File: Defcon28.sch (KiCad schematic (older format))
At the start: 10 parts

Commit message: Added regulators
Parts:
- added C? (x6): 1μF, symbol Device:C_Small
- added D?: LED_ALT, symbol Device:LED_ALT
- added R?: R_Small_US, symbol Device:R_Small_US
- added SW?: SW_SP4T, symbol Defcon28:SW_SP4T
- added U?: MCP1826S-1802E_DB, symbol Defcon28:MCP1826S-1802E_DB
- added U?: MCP1825ST-2502E_DB, symbol Defcon28:MCP1825ST-2502E_DB
- added U?: MCP1825ST-3302E_DB, symbol Defcon28:MCP1825ST-3302E_DB
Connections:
- net GND: now also C?.2, C?.2, C?.2, C?.2, C?.2, C?.2, D?.1 (K), U?.2 (GND), U?.2 (GND), U?.2 (GND)
- net VBUS: now also C?.1, C?.1, C?.1, R?.1, SW?.5, U?.1 (VIN), U?.1 (VIN), U?.1 (VIN)
- net VCC: now also SW?.3
- new net: D?.2 (A), R?.2
- new net +1V8: C?.1, SW?.1, U?.3 (VOUT)
- new net +2V5: C?.1, SW?.2, U?.3 (VOUT)
- new net +3V3: C?.1, SW?.4, U?.3 (VOUT)
- no-connect marks 7 -> 11
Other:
- moved on the sheet: D?

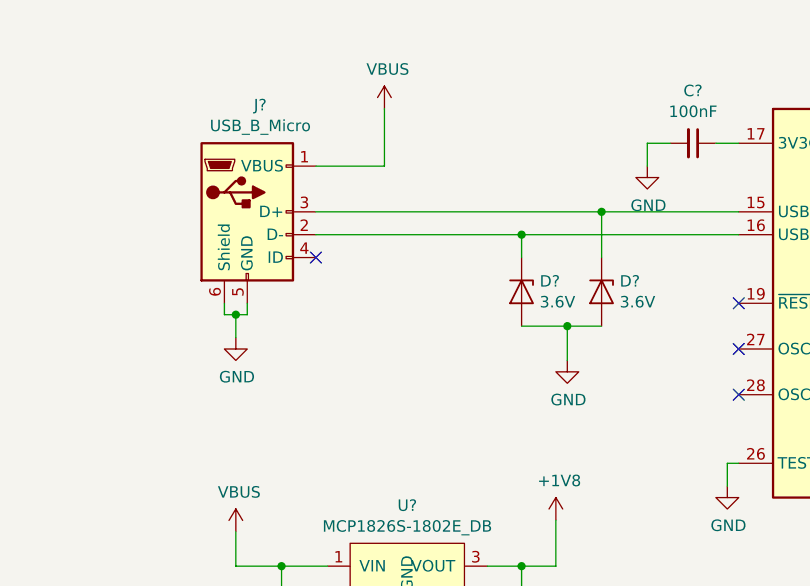
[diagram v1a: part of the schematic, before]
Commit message: Added input cap
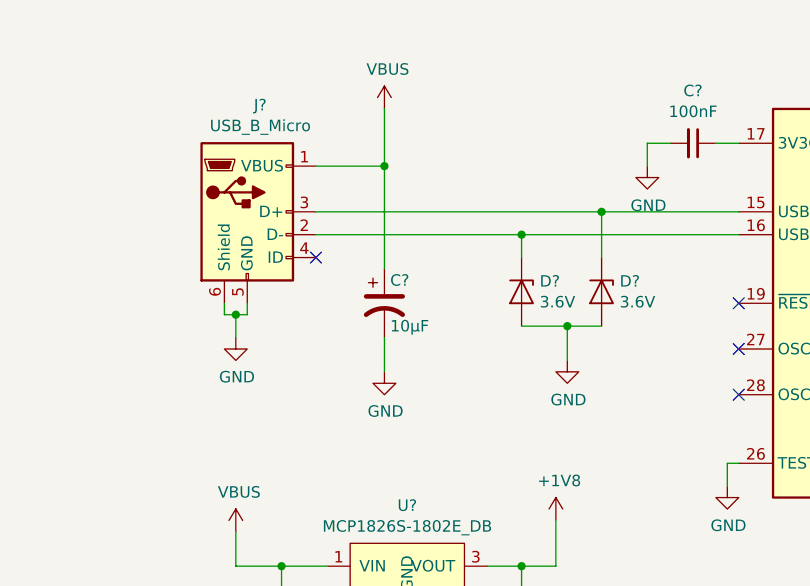
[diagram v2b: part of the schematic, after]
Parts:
- added C?: 10µF, symbol Device:CP1
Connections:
- net GND: now also C?.2
- net VBUS: now also C?.1
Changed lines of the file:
@@
 Wire Wire Line
 	3700 7350 3200 7350
+$Comp
+L Device:CP1 C?
+U 1 1 5E38AA29
+P 3100 3400
+F 0 "C?" H 3125 3500 50  0000 L CNN
+F 1 "10µF" H 3125 3300 50  0000 L CNN
+F 2 "" H 3100 3400 50  0001 C CNN
+F 3 "~" H 3100 3400 50  0001 C CNN
+	1    3100 3400
+	1    0    0    -1
+$EndComp
+Wire Wire Line
+	3100 3250 3100 2800
+Connection ~ 3100 2800
+$Comp
+L power:GND #PWR?
+U 1 1 5E38F14C
+P 3100 3700
+F 0 "#PWR?" H 3100 3450 50  0001 C CNN
+F 1 "GND" H 3105 3527 50  0000 C CNN
+F 2 "" H 3100 3700 50  0001 C CNN
+F 3 "" H 3100 3700 50  0001 C CNN
+	1    3100 3700
+	1    0    0    -1
+$EndComp
+Wire Wire Line
+	3100 3550 3100 3700
 $EndSCHEMATC

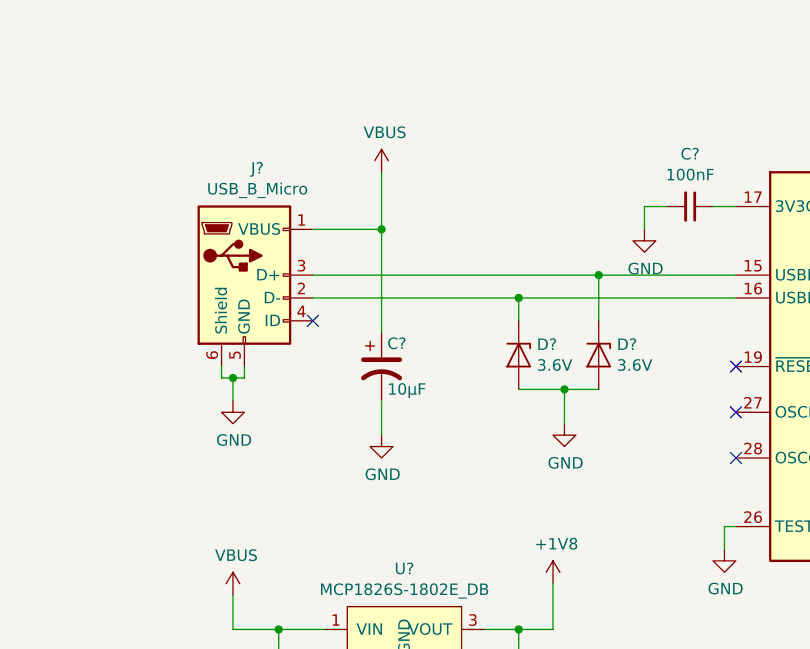
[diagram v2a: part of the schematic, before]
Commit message: Added ferrite to input.
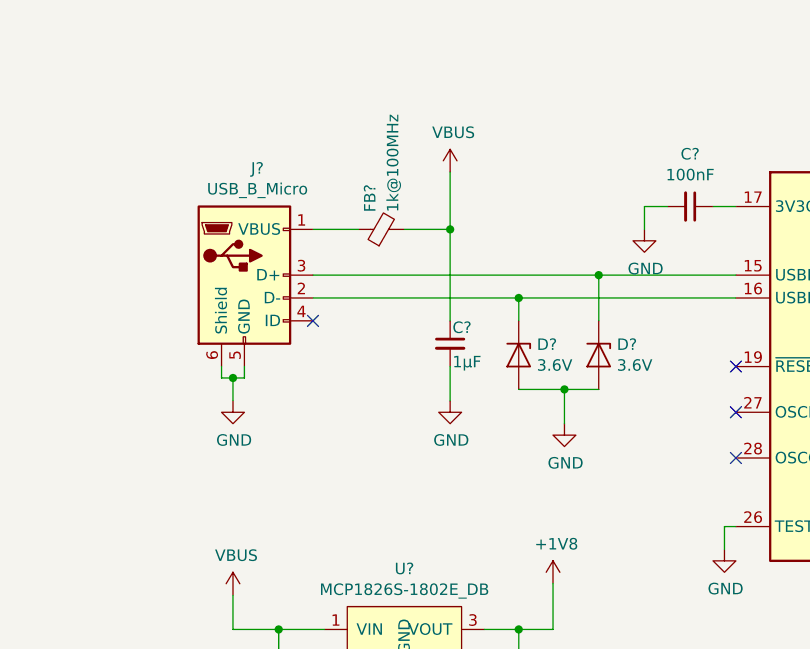
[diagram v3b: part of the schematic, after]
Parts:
- removed C?: 10µF, symbol Device:CP1
- added C?: 1µF, symbol Device:C_Small
- added FB?: 1k@100MHz, symbol Device:Ferrite_Bead_Small
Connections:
- net GND: now also C?.2
- net VBUS: now also C?.1, FB?.2; no longer J?.1 (VBUS)
- new net: FB?.1, J?.1 (VBUS)
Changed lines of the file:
@@
 L power:VBUS #PWR?
 U 1 1 5E32FD75
-P 3100 2550
-F 0 "#PWR?" H 3100 2400 50  0001 C CNN
-F 1 "VBUS" H 3115 2723 50  0000 C CNN
-F 2 "" H 3100 2550 50  0001 C CNN
-F 3 "" H 3100 2550 50  0001 C CNN
-	1    3100 2550
-	1    0    0    -1
-$EndComp
-Wire Wire Line
-	2800 2800 3100 2800
-Wire Wire Line
-	3100 2800 3100 2550
+P 3400 2550
+F 0 "#PWR?" H 3400 2400 50  0001 C CNN
+F 1 "VBUS" H 3415 2723 50  0000 C CNN
+F 2 "" H 3400 2550 50  0001 C CNN
+F 3 "" H 3400 2550 50  0001 C CNN
+	1    3400 2550
+	1    0    0    -1
+$EndComp
 $Comp
 L power:GND #PWR?
@@
 	3700 7350 3200 7350
 $Comp
-L Device:CP1 C?
-U 1 1 5E38AA29
-P 3100 3400
-F 0 "C?" H 3125 3500 50  0000 L CNN
-F 1 "10µF" H 3125 3300 50  0000 L CNN
-F 2 "" H 3100 3400 50  0001 C CNN
-F 3 "~" H 3100 3400 50  0001 C CNN
-	1    3100 3400
-	1    0    0    -1
-$EndComp
-Wire Wire Line
-	3100 3250 3100 2800
-Connection ~ 3100 2800
-$Comp
-L power:GND #PWR?
-U 1 1 5E38F14C
-P 3100 3700
-F 0 "#PWR?" H 3100 3450 50  0001 C CNN
-F 1 "GND" H 3105 3527 50  0000 C CNN
-F 2 "" H 3100 3700 50  0001 C CNN
-F 3 "" H 3100 3700 50  0001 C CNN
-	1    3100 3700
-	1    0    0    -1
-$EndComp
-Wire Wire Line
-	3100 3550 3100 3700
+L Device:Ferrite_Bead_Small FB?
+U 1 1 5E39E86F
+P 3100 2800
+F 0 "FB?" H 3175 2850 50  0000 L CNN
+F 1 "1k@100MHz" H 3175 2750 50  0000 L CNN
+F 2 "" V 3030 2800 50  0001 C CNN
+F 3 "~" H 3100 2800 50  0001 C CNN
+	1    3100 2800
+	0    -1   -1   0
+$EndComp
+Wire Wire Line
+	2800 2800 3000 2800
+Wire Wire Line
+	3200 2800 3400 2800
+Wire Wire Line
+	3400 2800 3400 2550
+$Comp
+L Device:C_Small C?
+U 1 1 5E3A6B46
+P 3400 3300
+F 0 "C?" H 3410 3370 50  0000 L CNN
+F 1 "1µF" H 3410 3220 50  0000 L CNN
+F 2 "" H 3400 3300 50  0001 C CNN
+F 3 "~" H 3400 3300 50  0001 C CNN
+	1    3400 3300
+	1    0    0    -1
+$EndComp
+Wire Wire Line
+	3400 3200 3400 2800
+Connection ~ 3400 2800
+$Comp
+L power:GND #PWR?
+U 1 1 5E3AAD2D
+P 3400 3550
+F 0 "#PWR?" H 3400 3300 50  0001 C CNN
+F 1 "GND" H 3405 3377 50  0000 C CNN
+F 2 "" H 3400 3550 50  0001 C CNN
+F 3 "" H 3400 3550 50  0001 C CNN
+	1    3400 3550
+	1    0    0    -1
+$EndComp
+Wire Wire Line
+	3400 3550 3400 3400
 $EndSCHEMATC

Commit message: Changed switch to DP4T
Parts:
- added D6: LED_GREEN, LED_SMD:LED_0805_2012Metric_Castellated, symbol Device:LED_ALT
- added D7: LED_YELLOW, LED_SMD:LED_0805_2012Metric_Castellated, symbol Device:LED_ALT
- added D8: LED_ORANGE, LED_SMD:LED_0805_2012Metric_Castellated, symbol Device:LED_ALT
- added D9: LED_RED, LED_SMD:LED_0805_2012Metric_Castellated, symbol Device:LED_ALT
- added R4: 62R, Resistor_SMD:R_0805_2012Metric_Pad1.15x1.40mm_HandSolder, symbol Device:R_Small_US
- added R5, R6, R7: 100R, Resistor_SMD:R_0805_2012Metric_Pad1.15x1.40mm_HandSolder, symbol Device:R_Small_US
- C1, C2, C3, C4, C5, C6, C7, C8: renamed from C?; footprint (none) -> Capacitor_SMD:C_0805_2012Metric_Pad1.15x1.40mm_HandSolder
- D1: renamed from D?; value LED_ALT -> LED_RED; footprint (none) -> LED_SMD:LED_0805_2012Metric_Castellated
- D2, D3: renamed from D?; footprint (none) -> Diode_SMD:D_MiniMELF
- D4: renamed from D?; value LED_ALT -> LED_YELLOW; footprint (none) -> LED_SMD:LED_0805_2012Metric_Castellated
- D5: renamed from D?; value LED_ALT -> LED_GREEN; footprint (none) -> LED_SMD:LED_0805_2012Metric_Castellated
- FB1: renamed from FB?; footprint (none) -> Inductor_SMD:L_0805_2012Metric
- J1: renamed from J?; footprint (none) -> Connector_USB:USB_Micro-B_Amphenol_10103594-0001LF_Horizontal
- J2: renamed from J?; Vendor (none) -> Digikey; Vendor Part # (none) -> SAM15786-ND
- R1, R2: renamed from R?; value R_Small_US -> 100R; footprint (none) -> Resistor_SMD:R_0805_2012Metric_Pad1.15x1.40mm_HandSolder
- R3: renamed from R?; value R_Small_US -> 62R; footprint (none) -> Resistor_SMD:R_0805_2012Metric_Pad1.15x1.40mm_HandSolder
- SW1: renamed from SW?; symbol Defcon28:SW_SP4T -> Defcon28:SW_DP4T; Part # 103-5043-EV -> 688-SSSS224100
- U1, U2, U3: renamed from U?; footprint (none) -> Package_TO_SOT_SMD:SOT-223-3_TabPin2
- gave numbers to parts that had none: 1
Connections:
- net GND: now also D6.1 (K), D7.1 (K), D8.1 (K), D9.1 (K)
- net VBUS: now also SW1.8
- new net: D6.2 (A), R4.2
- new net: D7.2 (A), R5.2
- new net: D8.2 (A), R6.2
- new net: D9.2 (A), R7.2
- new net LED_1.8: R4.1, SW1.6
- new net LED_2.5: R5.1, SW1.7
- new net LED_3.3: R6.1, SW1.9
- new net LED_5.0: R7.1, SW1.10
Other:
- moved on the sheet: C1, C2, C3, C4, C5, C6, C7, C8, D1, D2, D3, D4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

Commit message: Title
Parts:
- U1: PArt # (none) -> 579-MCP1826S-1802EDB; Vendor (none) -> Mouser
- U2: Part # (none) -> 579-MCP1825ST2502EDB; Vendor (none) -> Mouser
- U3: Part # (none) -> 579-MCP1825ST3302EDB; Vendor (none) -> Mouser
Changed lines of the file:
@@
 encoding utf-8
 Sheet 1 1
-Title ""
-Date ""
-Rev ""
-Comp ""
+Title "The Device"
+Date "2020-02-27"
+Rev "0.1"
+Comp "FC801"
 Comment1 ""
 Comment2 ""
@@
 F 2 "Package_TO_SOT_SMD:SOT-223-3_TabPin2" H 3100 3650 50  0001 C CNN
 F 3 "https://www.mouser.com/datasheet/2/268/22057B-474578.pdf" H 3100 3650 50  0001 C CNN
+F 4 "Mouser" H 3100 3650 50  0001 C CNN "Vendor"
+F 5 "579-MCP1826S-1802EDB " H 3100 3650 50  0001 C CNN "PArt #"
 	1    3100 3650
 	1    0    0    -1
@@
 F 2 "Package_TO_SOT_SMD:SOT-223-3_TabPin2" H 3100 4800 50  0001 C CNN
 F 3 "https://www.mouser.com/datasheet/2/268/22056b-475378.pdf" H 3100 4800 50  0001 C CNN
+F 4 "Mouser" H 3100 4800 50  0001 C CNN "Vendor"
+F 5 "579-MCP1825ST2502EDB" H 3100 4800 50  0001 C CNN "Part #"
 	1    3100 4800
 	1    0    0    -1
@@
 F 2 "Package_TO_SOT_SMD:SOT-223-3_TabPin2" H 3100 6050 50  0001 C CNN
 F 3 "https://www.mouser.com/datasheet/2/268/22056b-475378.pdf" H 3100 6050 50  0001 C CNN
+F 4 "Mouser" H 3100 6050 50  0001 C CNN "Vendor"
+F 5 "579-MCP1825ST3302EDB" H 3100 6050 50  0001 C CNN "Part #"
 	1    3100 6050
 	1    0    0    -1
